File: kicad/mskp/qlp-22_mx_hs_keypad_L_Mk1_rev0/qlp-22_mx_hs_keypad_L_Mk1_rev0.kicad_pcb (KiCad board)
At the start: 2 copper layers, 162 x 112 mm, 28 parts, among them J1 Conn_01x12_Socket, SW0 Switch, SW1 Switch, SW10 Switch, SW2 Switch, SW3 Switch, SW4 Switch, SW5 Switch, SW6 Switch, SW7 Switch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

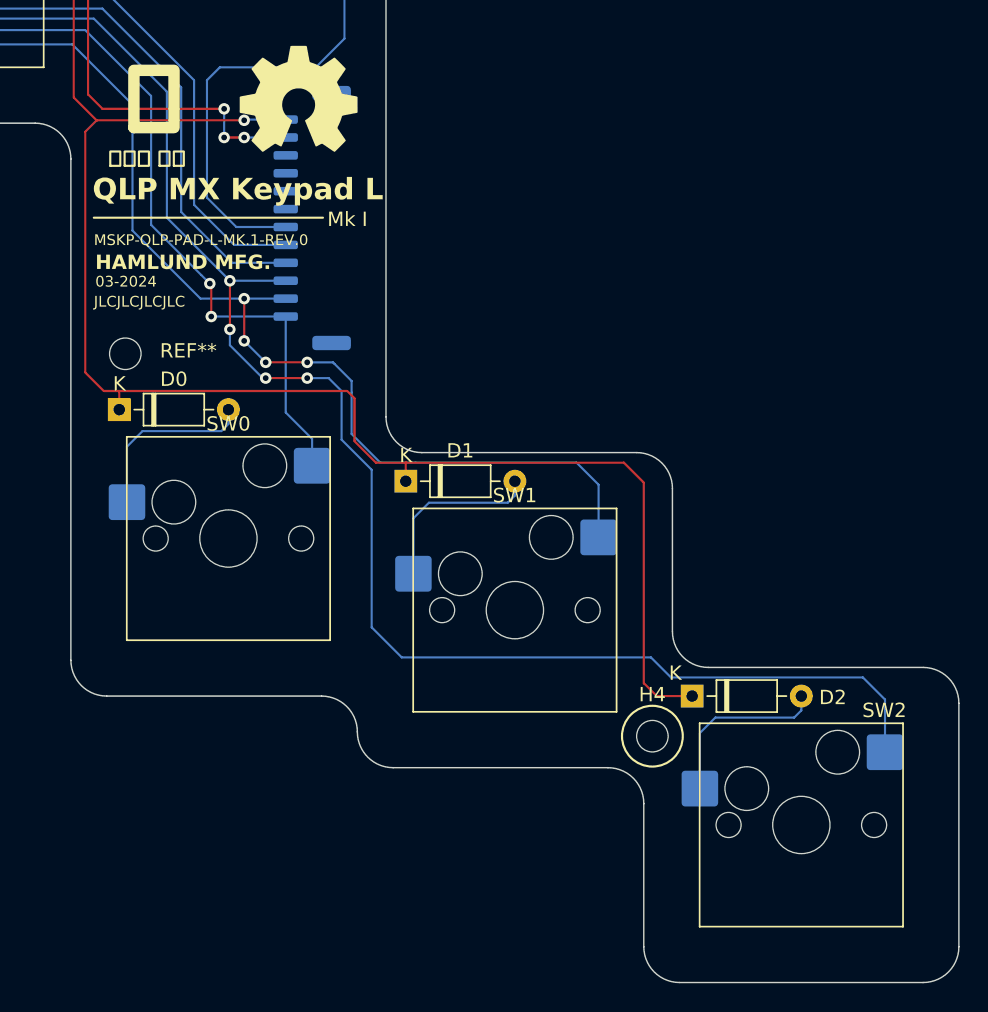
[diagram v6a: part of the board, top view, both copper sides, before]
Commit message: Minor silkscreen and makes connector flush with PCB edge
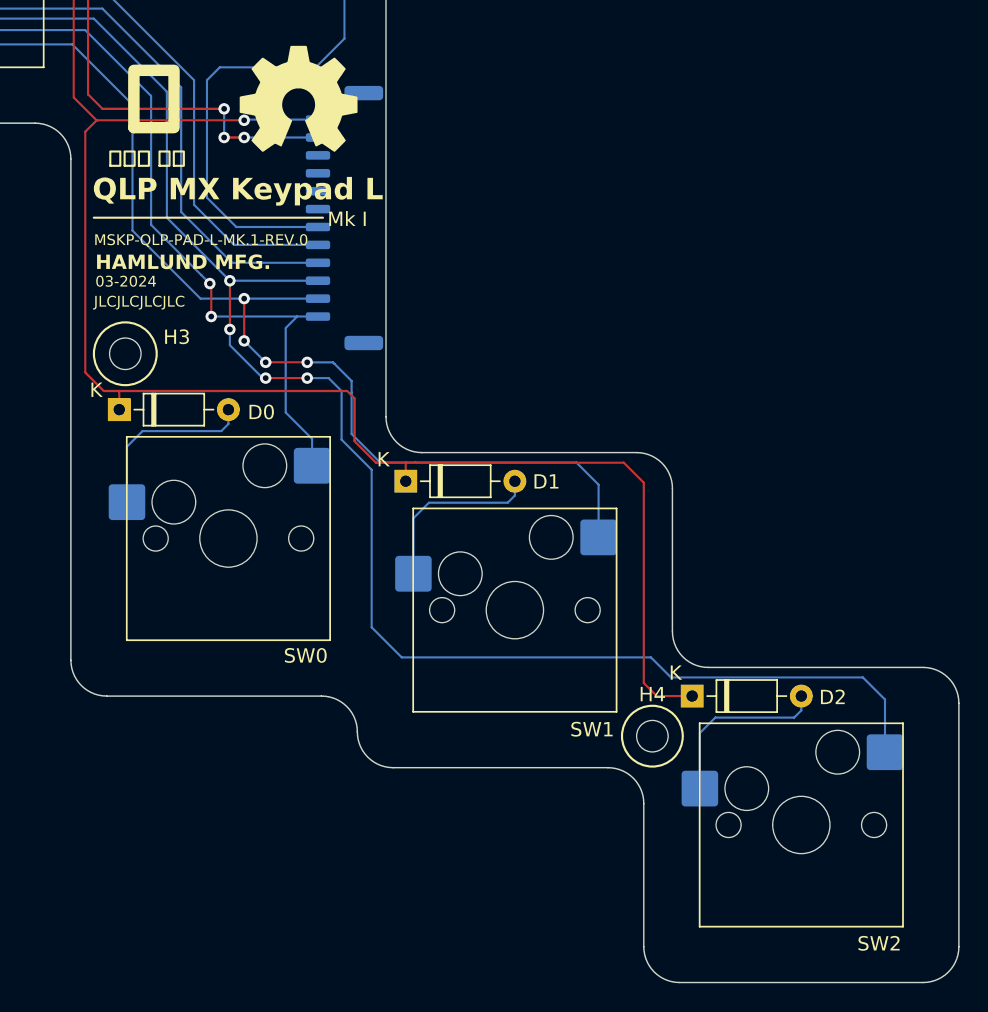
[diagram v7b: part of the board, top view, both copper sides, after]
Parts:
- moved J1 2.25 mm to (176.6, 87.1)
- renumbered REF** to H3
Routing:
- net Net-(J1-Pin_12): track 129.4 -> 132.0 mm
- net Net-(J1-Pin_8): track 56.4 -> 58.7 mm
- net Net-(J1-Pin_7): track 41.5 -> 43.7 mm
- net Net-(J1-Pin_11): track 133.2 -> 135.4 mm
- net Net-(J1-Pin_10): track 150.1 -> 152.4 mm
- net Net-(D10-K): track 168.8 -> 171.0 mm
- net Net-(D0-K): track 182.6 -> 184.8 mm
- net Net-(J1-Pin_9): track 89.6 -> 91.9 mm

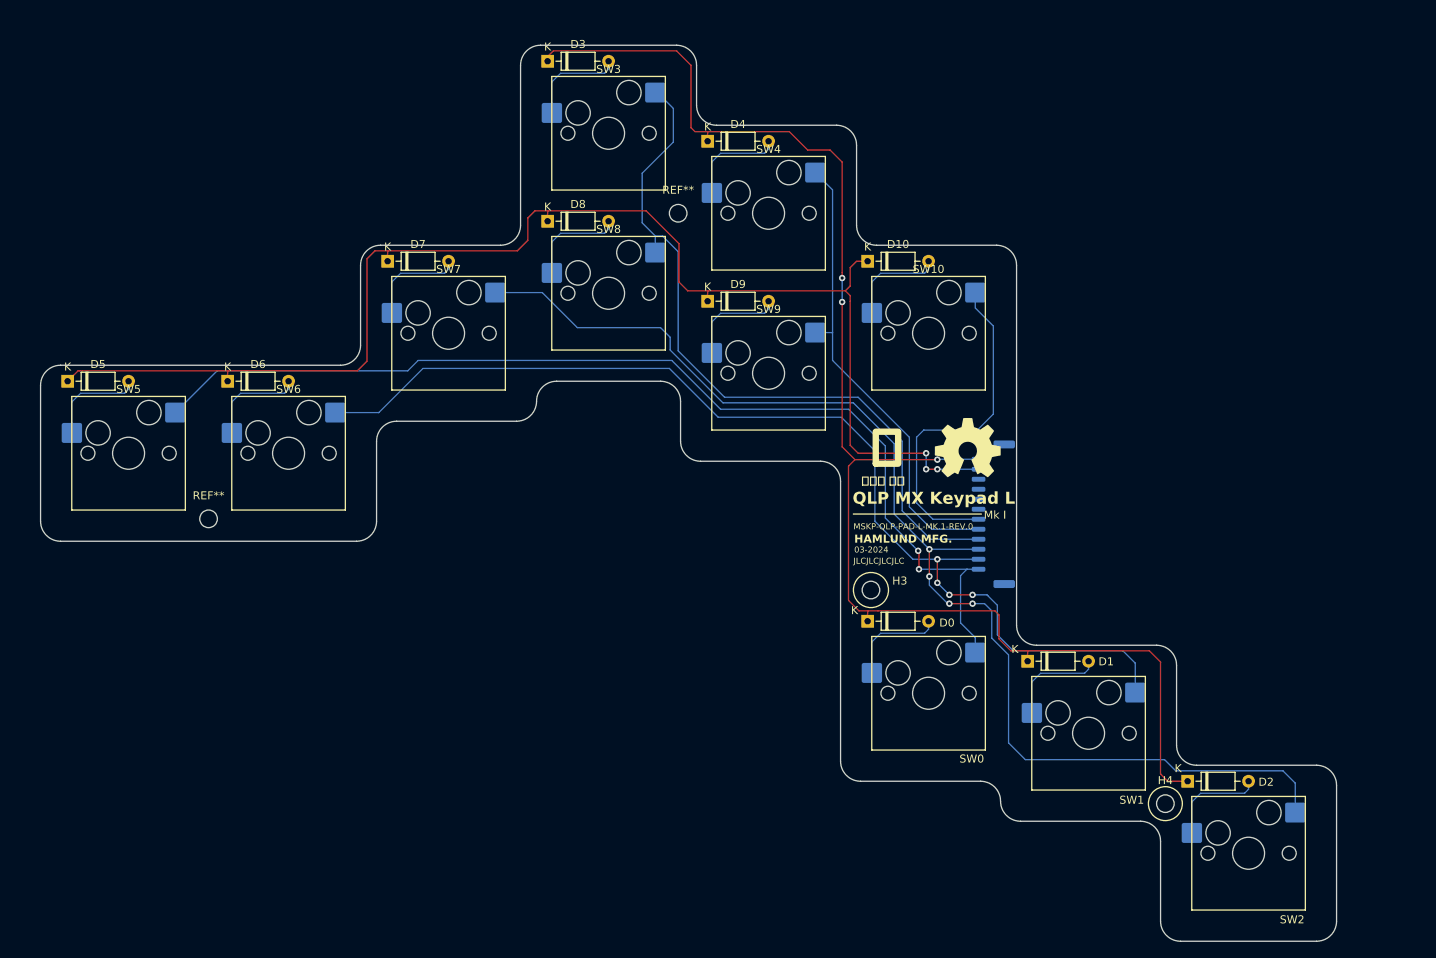
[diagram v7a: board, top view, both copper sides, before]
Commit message: Finalizes mskp pcbs before first run
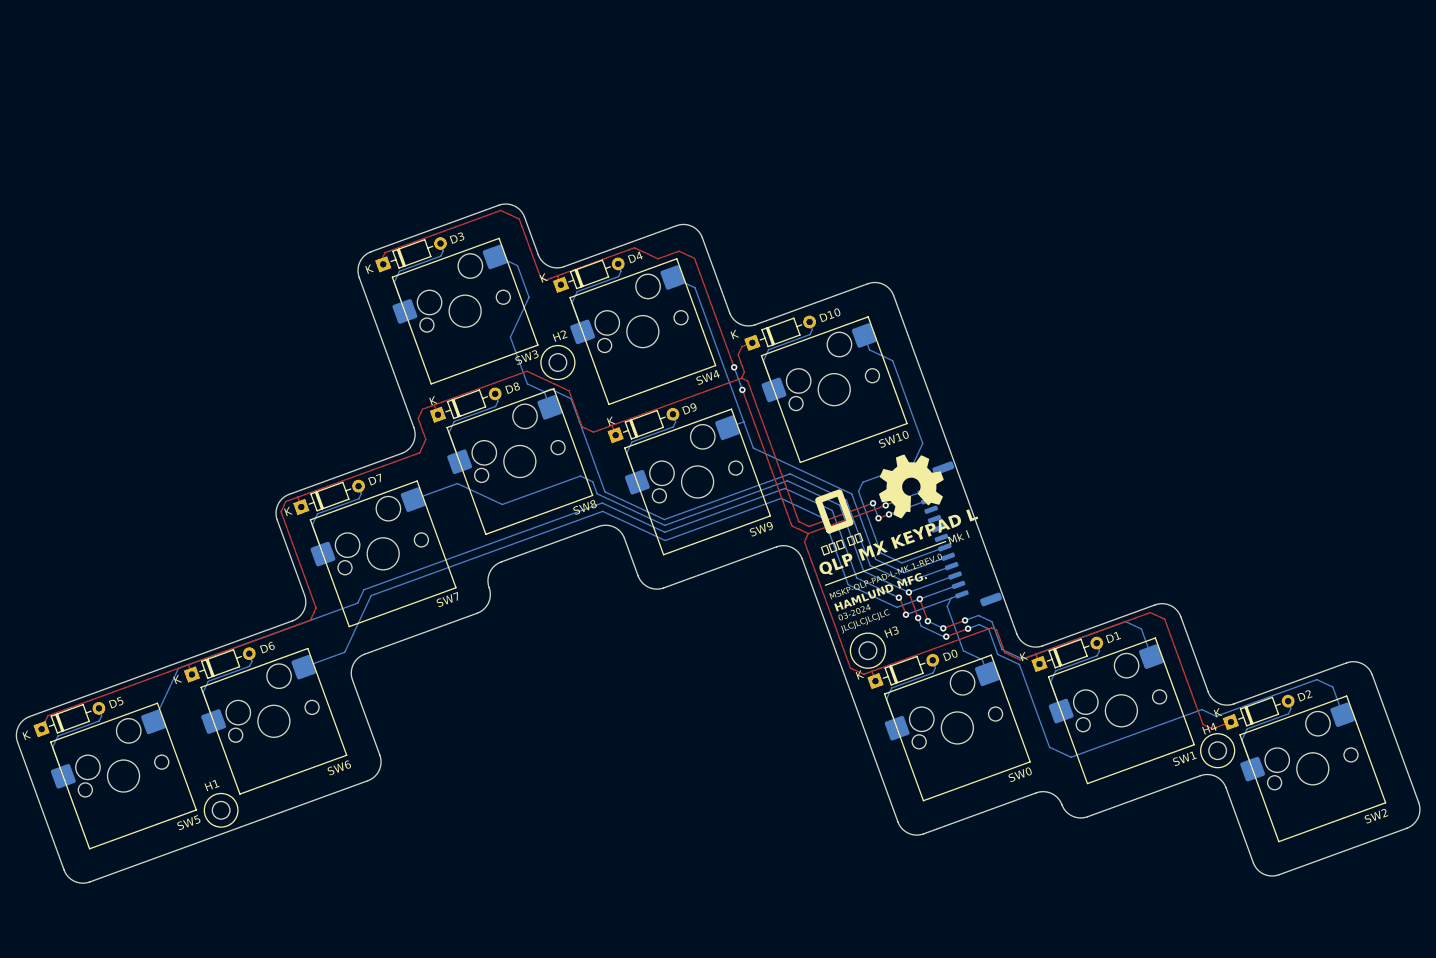
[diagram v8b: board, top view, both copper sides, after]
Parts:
- moved D5 43.6 mm to (57.6, 114.0), turned to 20 degrees
- moved SW5 40.4 mm to (67.9, 119.8), turned to 20 degrees
- moved D6 36.9 mm to (76.4, 107.2), turned to 20 degrees
- moved H1 36.5 mm to (80.1, 124.1), turned to 20 degrees
- moved SW6 33.6 mm to (86.7, 113.0), turned to 20 degrees
- moved D3 32.7 mm to (100.3, 55.9), turned to 20 degrees
- moved D7 32.6 mm to (90.1, 86.2), turned to 20 degrees
- moved SW7 28.8 mm to (100.3, 92.1), turned to 20 degrees
- moved SW3 28.6 mm to (110.6, 61.7), turned to 20 degrees
- moved D8 27.8 mm to (107.2, 74.7), turned to 20 degrees
- moved D4 25.7 mm to (122.5, 58.4), turned to 20 degrees
- moved H2 24.0 mm to (122.2, 68.2), turned to 20 degrees
- moved SW8 23.8 mm to (117.4, 80.5), turned to 20 degrees
- moved SW4 21.6 mm to (132.8, 64.3), turned to 20 degrees
- moved D9 20.3 mm to (129.4, 77.2), turned to 20 degrees
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- renumbered REF** to H1, REF** to H2
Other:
- board size 162 x 112 mm -> 175.4 x 84.9 mm
- board text added: "CONTROL MODULE"
- board text added: "QLP MX KEYPAD L"
- board text added: "S0:0"
- board text added: "S0:1"
- board text added: "S0:2"
- board text added: "S0:3"
- board text added: "S0:4"
- board text added: "S1:0"
- board text added: "S1:1"
- board text added: "S1:2"
- board text added: "S1:3"
- board text added: "S1:4"
- board text added: "S1:5"
- board text removed: "QLP MX Keypad L"
